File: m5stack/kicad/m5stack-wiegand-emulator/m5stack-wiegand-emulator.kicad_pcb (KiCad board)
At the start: 2 copper layers, 50 x 50 mm, 21 parts, among them J1 2x15 socket header, J2 2x15 pin header, J3 1x5 female, U2 ISOW7841, U3 SN74LVC2G126-EP, U4 TPS62906DRL, U5 SN74AHCT1G125

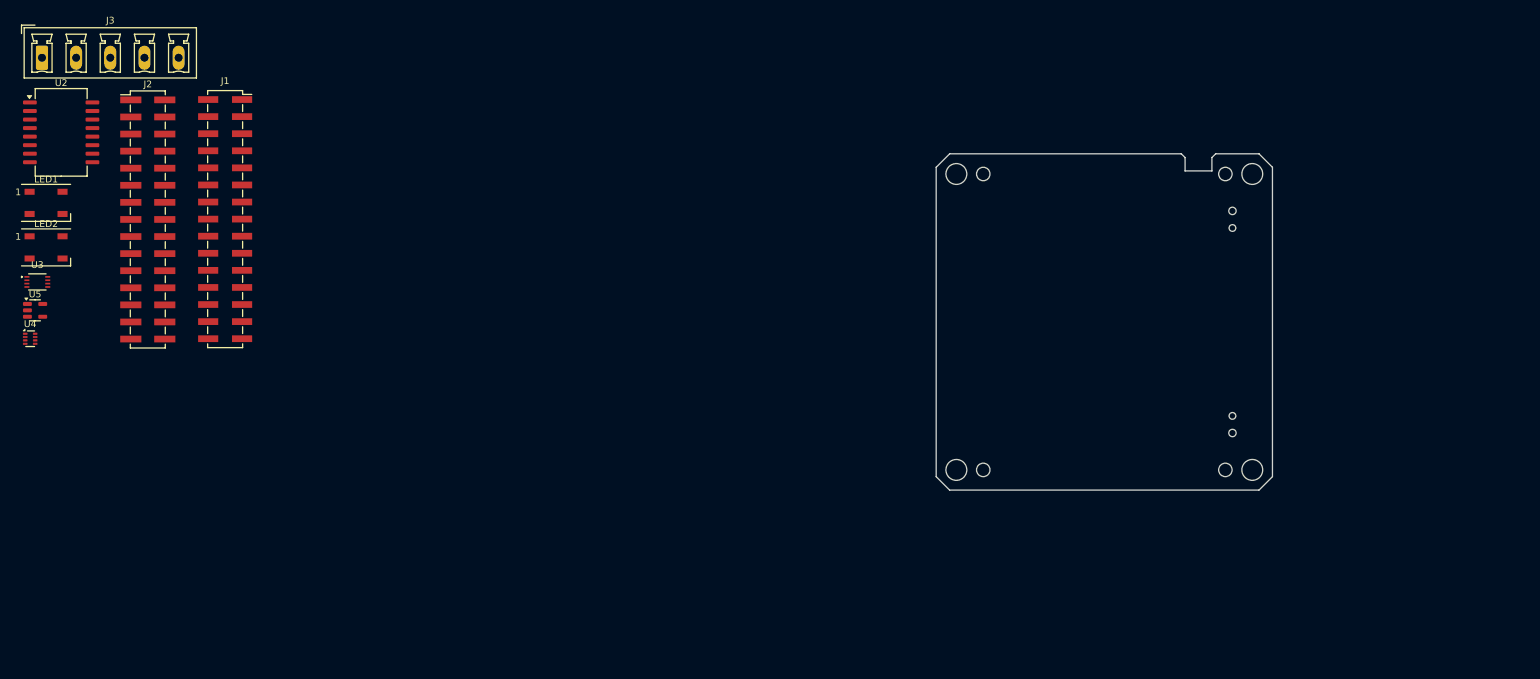
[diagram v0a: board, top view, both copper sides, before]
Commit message: M5: placed J1/J2 connectors
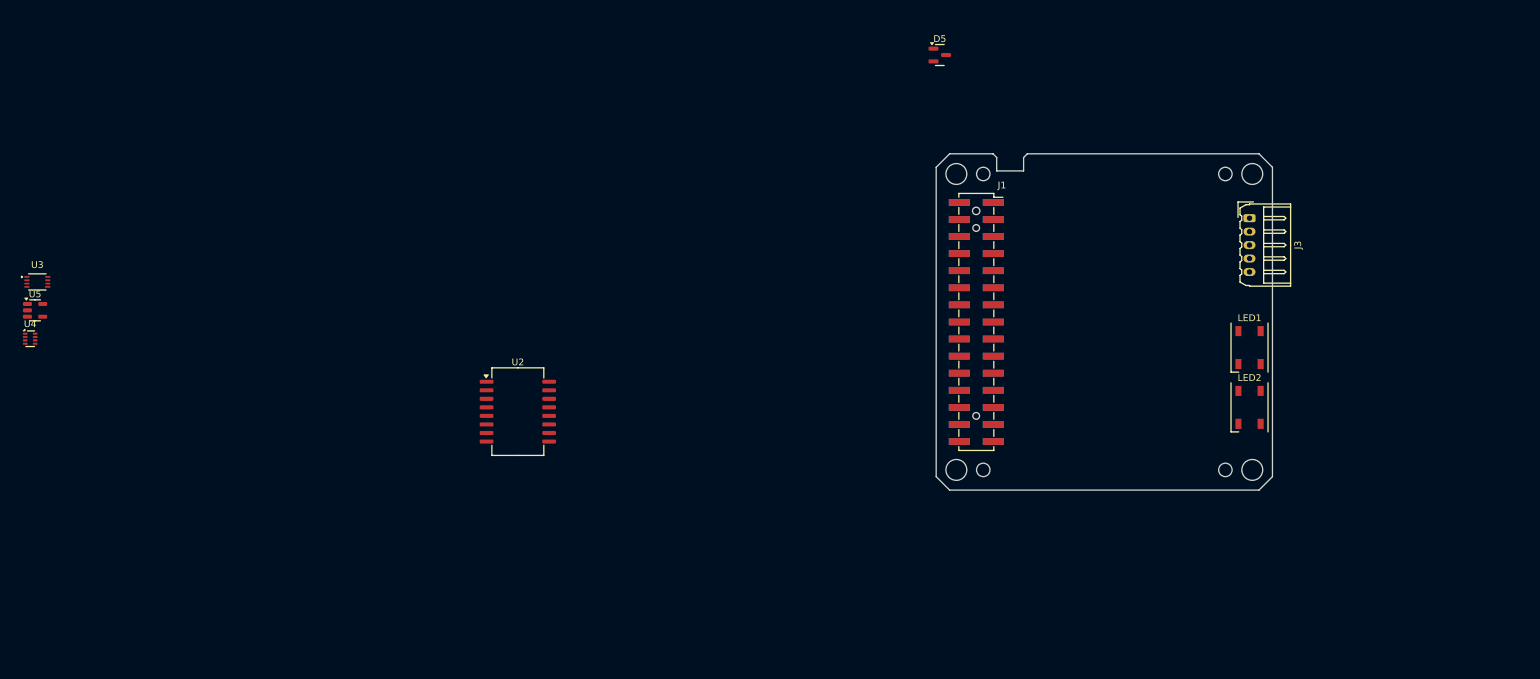
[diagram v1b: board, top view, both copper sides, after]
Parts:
- removed the REF** at (133.3, 105.4)
- added D5: BAT54S, Package_TO_SOT_SMD:SOT-23, F.Cu at (89.8, 49.2)
- J2: moved to B.Cu
- J3: footprint Connector_Phoenix_MC_HighVoltage:PhoenixContact_MCV_1,5_5-G-5.08_1x05_P5.08mm_Vertical -> Connector_Molex:Molex_Micro-Latch_53254-0570_1x05_P2.00mm_Horizontal
- moved J3 181.1 mm to (135.9, 73.5), turned to -90 degrees
- moved LED2 180.5 mm to (135.9, 101.6), turned to -90 degrees
- moved LED1 180.2 mm to (135.9, 92.7), turned to -90 degrees
- moved J2 124.1 mm to (95.3, 88.9), turned to 180 degrees
- moved J1 112.7 mm to (95.3, 88.9)
- moved U2 79.6 mm to (27.1, 102.2)
- moved REF** 38.1 mm to (95.2, 102.9)
- moved REF** 38.1 mm to (95.2, 74.9)
- moved REF** 38.1 mm to (95.2, 72.4)
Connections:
- J1 pad 1: GND -> /ADC1
- J1 pad 10: /DAC1 -> /MISO
- J1 pad 11: /SCLK -> /3V3
- J1 pad 12: /3V3 -> /SCLK
- J1 pad 13: /RXD1 -> /TXD1
- J1 pad 14: /TXD1 -> /RXD1
- J1 pad 15: /RXD2 -> /TXD2
- J1 pad 16: /TXD2 -> /RXD2
- J1 pad 17: /SDA -> /SCL
- J1 pad 18: /SCL -> /SDA
- J1 pad 19: /IO6 -> /IO7
- J1 pad 2: /ADC1 -> GND
- J1 pad 20: /IO7 -> /IO6
- J1 pad 21: /IO8 -> /IO9
- J1 pad 22: /IO9 -> /IO8
- J1 pad 23: /IO10 -> /IO11
- J1 pad 24: /IO11 -> /IO10
- J1 pad 25: /HPWR -> /ADC0
- J1 pad 26: /ADC0 -> /HPWR
- J1 pad 27: /HPWR -> /5VDC
- J1 pad 28: /5VDC -> /HPWR
- J1 pad 29: /HPWR -> /BATTERY
- J1 pad 3: GND -> /ADC2
- J1 pad 30: /BATTERY -> /HPWR
- J1 pad 4: /ADC2 -> GND
- J1 pad 5: GND -> /RESET
- J1 pad 6: /RESET -> GND
- J1 pad 7: /MOSI -> /DAC0
- J1 pad 8: /DAC0 -> /MOSI
- J1 pad 9: /MISO -> /DAC1
- J2 pad 1: GND -> /ADC1
- J2 pad 10: /DAC1 -> /MISO
- J2 pad 11: /SCLK -> /3V3
- J2 pad 12: /3V3 -> /SCLK
- J2 pad 13: /RXD1 -> /TXD1
- J2 pad 14: /TXD1 -> /RXD1
- J2 pad 15: /RXD2 -> /TXD2
- J2 pad 16: /TXD2 -> /RXD2
- J2 pad 17: /SDA -> /SCL
- J2 pad 18: /SCL -> /SDA
- J2 pad 19: /IO6 -> /IO7
- J2 pad 2: /ADC1 -> GND
- J2 pad 20: /IO7 -> /IO6
- J2 pad 21: /IO8 -> /IO9
- J2 pad 22: /IO9 -> /IO8
- J2 pad 23: /IO10 -> /IO11
- J2 pad 24: /IO11 -> /IO10
- J2 pad 25: /HPWR -> /ADC0
- J2 pad 26: /ADC0 -> /HPWR
- J2 pad 27: /HPWR -> /5VDC
- J2 pad 28: /5VDC -> /HPWR
- J2 pad 29: /HPWR -> /BATTERY
- J2 pad 3: GND -> /ADC2
- J2 pad 30: /BATTERY -> /HPWR
- J2 pad 4: /ADC2 -> GND
- J2 pad 5: GND -> /RESET
- J2 pad 6: /RESET -> GND
- J2 pad 7: /MOSI -> /DAC0
- J2 pad 8: /DAC0 -> /MOSI
- J2 pad 9: /MISO -> /DAC1
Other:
- outline, holes or cut-outs redrawn

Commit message: M5: adding missing footprints
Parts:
- removed LED2: WS2812B, LED_SMD:LED_WS2812B_PLCC4_5.0x5.0mm_P3.2mm
- added C2: 10nF, Capacitor_SMD:C_0805_2012Metric_Pad1.18x1.45mm_HandSolder, F.Cu at (113.0, 82.5)
- added C3: 10nF, Capacitor_SMD:C_0805_2012Metric_Pad1.18x1.45mm_HandSolder, F.Cu at (113.0, 85.1)
- added C4: 0.1uF, Capacitor_SMD:C_0805_2012Metric_Pad1.18x1.45mm_HandSolder, F.Cu at (108.0, 82.5)
- added C5: 0.1uF, Capacitor_SMD:C_0805_2012Metric_Pad1.18x1.45mm_HandSolder, F.Cu at (108.0, 85.1)
- added C6: 0.1uF, Capacitor_SMD:C_0805_2012Metric_Pad1.18x1.45mm_HandSolder, F.Cu at (102.9, 85.1)
- added C7: 0.1uF, Capacitor_SMD:C_0805_2012Metric_Pad1.18x1.45mm_HandSolder, F.Cu at (102.9, 82.5)
- added F1: Polyfuse_Small, Fuse:Fuse_Littelfuse-NANO2-451_453, F.Cu at (132.1, 77.6)
- added JP1: Jumper_2_Bridged, Connector_PinHeader_1.27mm:PinHeader_1x02_P1.27mm_Vertical, F.Cu at (102.9, 71.1)
- added JP2: Jumper_3_Bridged12, Connector_PinHeader_1.27mm:PinHeader_1x03_P1.27mm_Vertical, F.Cu at (101.6, 91.4)
- added JP3: Jumper_2_Bridged, Connector_PinHeader_1.27mm:PinHeader_1x02_P1.27mm_Vertical, F.Cu at (102.9, 74.9)
- added JP4: Jumper_3_Bridged12, Connector_PinHeader_1.27mm:PinHeader_1x03_P1.27mm_Vertical, F.Cu at (101.6, 99.1)
- added JP5: Jumper_3_Bridged12, Connector_PinHeader_1.27mm:PinHeader_1x03_P1.27mm_Vertical, F.Cu at (118.1, 83.8)
- added JP6: Jumper_2_Bridged, Connector_PinHeader_1.27mm:PinHeader_1x02_P1.27mm_Vertical, F.Cu at (132.1, 71.1)
- added JP7: Jumper_3_Bridged12, Connector_PinHeader_1.27mm:PinHeader_1x03_P1.27mm_Vertical, F.Cu at (124.5, 83.8)
- added R1: 10k, Resistor_SMD:R_Array_Convex_5x1206, F.Cu at (128.3, 90.2)
- added R10: 470, Resistor_SMD:R_0805_2012Metric_Pad1.20x1.40mm_HandSolder, F.Cu at (133.1, 92.7)
- added R11: 470, Resistor_SMD:R_0805_2012Metric_Pad1.20x1.40mm_HandSolder, F.Cu at (137.2, 87.6)
- added R12: 470, Resistor_SMD:R_0805_2012Metric_Pad1.20x1.40mm_HandSolder, F.Cu at (137.2, 90.2)
- added R13: 10, Resistor_SMD:R_0805_2012Metric_Pad1.20x1.40mm_HandSolder, F.Cu at (137.2, 92.7)
- added R14: 100k, Resistor_SMD:R_0805_2012Metric_Pad1.20x1.40mm_HandSolder, F.Cu at (121.9, 73.7)
- added R15: 100k, Resistor_SMD:R_0805_2012Metric_Pad1.20x1.40mm_HandSolder, F.Cu at (121.7, 76.2)
- added R16: 27k, Resistor_SMD:R_0805_2012Metric_Pad1.20x1.40mm_HandSolder, F.Cu at (121.9, 78.7)
- added R4: 470, Resistor_SMD:R_0805_2012Metric_Pad1.20x1.40mm_HandSolder, F.Cu at (128.3, 109.2)
- added R7: 10k, Resistor_SMD:R_0805_2012Metric_Pad1.20x1.40mm_HandSolder, F.Cu at (128.3, 105.4)
- added R8: 10k, Resistor_SMD:R_0805_2012Metric_Pad1.20x1.40mm_HandSolder, F.Cu at (133.1, 87.6)
- added R9: 10k, Resistor_SMD:R_0805_2012Metric_Pad1.20x1.40mm_HandSolder, F.Cu at (133.1, 90.2)
- added TP1: TestPoint, TestPoint:TestPoint_THTPad_1.0x1.0mm_Drill0.5mm, F.Cu at (129.5, 64.8)
- added TP2: TestPoint, TestPoint:TestPoint_THTPad_1.0x1.0mm_Drill0.5mm, F.Cu at (119.4, 64.8)
- added TP3: TestPoint, TestPoint:TestPoint_THTPad_1.0x1.0mm_Drill0.5mm, F.Cu at (125.7, 64.8)
- added TP4: TestPoint, TestPoint:TestPoint_THTPad_1.0x1.0mm_Drill0.5mm, F.Cu at (100.3, 111.8)
- added U1: RP2040, uhppoted:RP2040-TINY, F.Cu at (114.3, 100.3)
- moved U5 179.5 mm to (134.6, 96.5)
- moved U4 168.5 mm to (121.4, 67.8)
- moved U3 166.7 mm to (121.9, 71.1)
- moved U2 89.4 mm to (111.8, 73.7)
- moved D5 63.3 mm to (129.2, 98.7)
- moved LED1 11.4 mm to (135.5, 104.1)
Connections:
- LED1 pad 2: Net-(LED1-DOUT) -> unconnected-(LED1-DOUT-Pad2)
- U4 pad 2: Net-(JP9-A) -> GND
- U4 pad 7: Net-(JP8-A) -> Net-(D1-K)

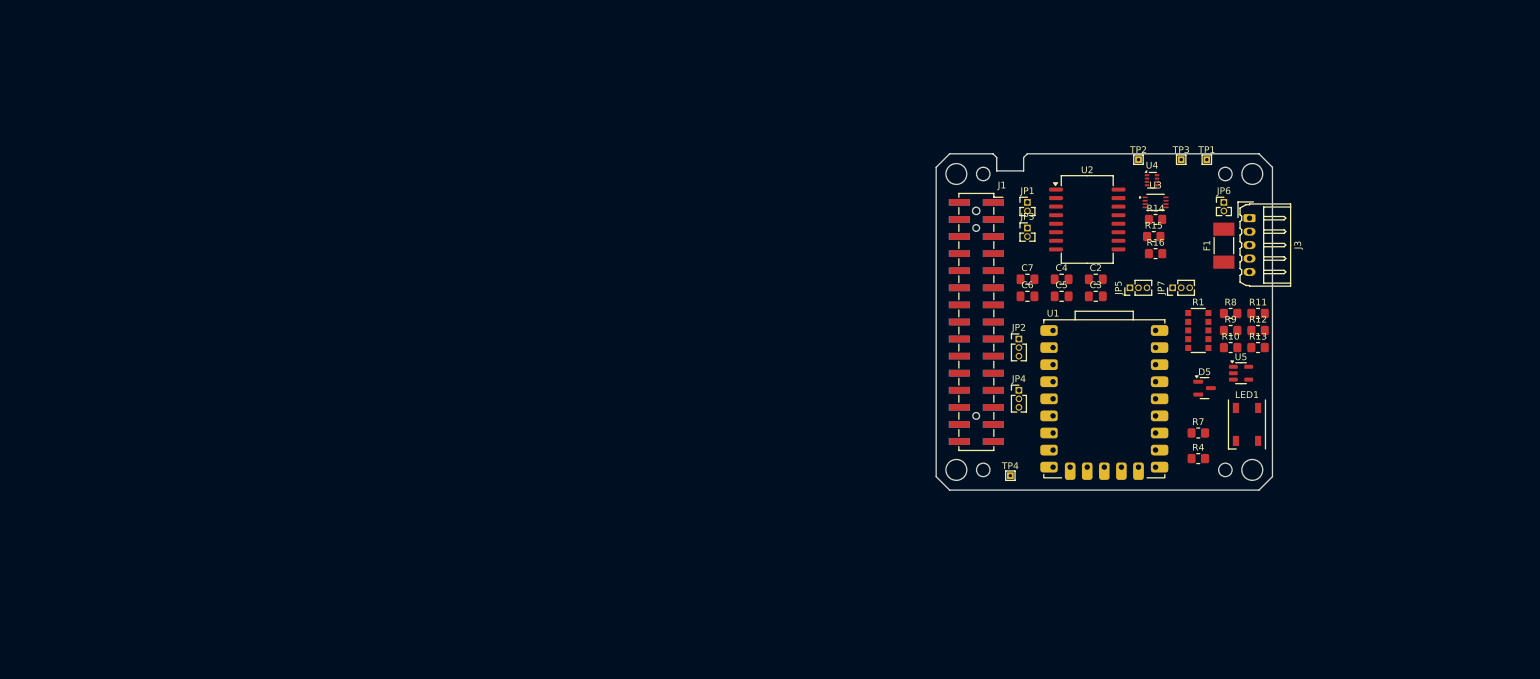
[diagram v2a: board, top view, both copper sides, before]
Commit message: M5: shuffling footprints
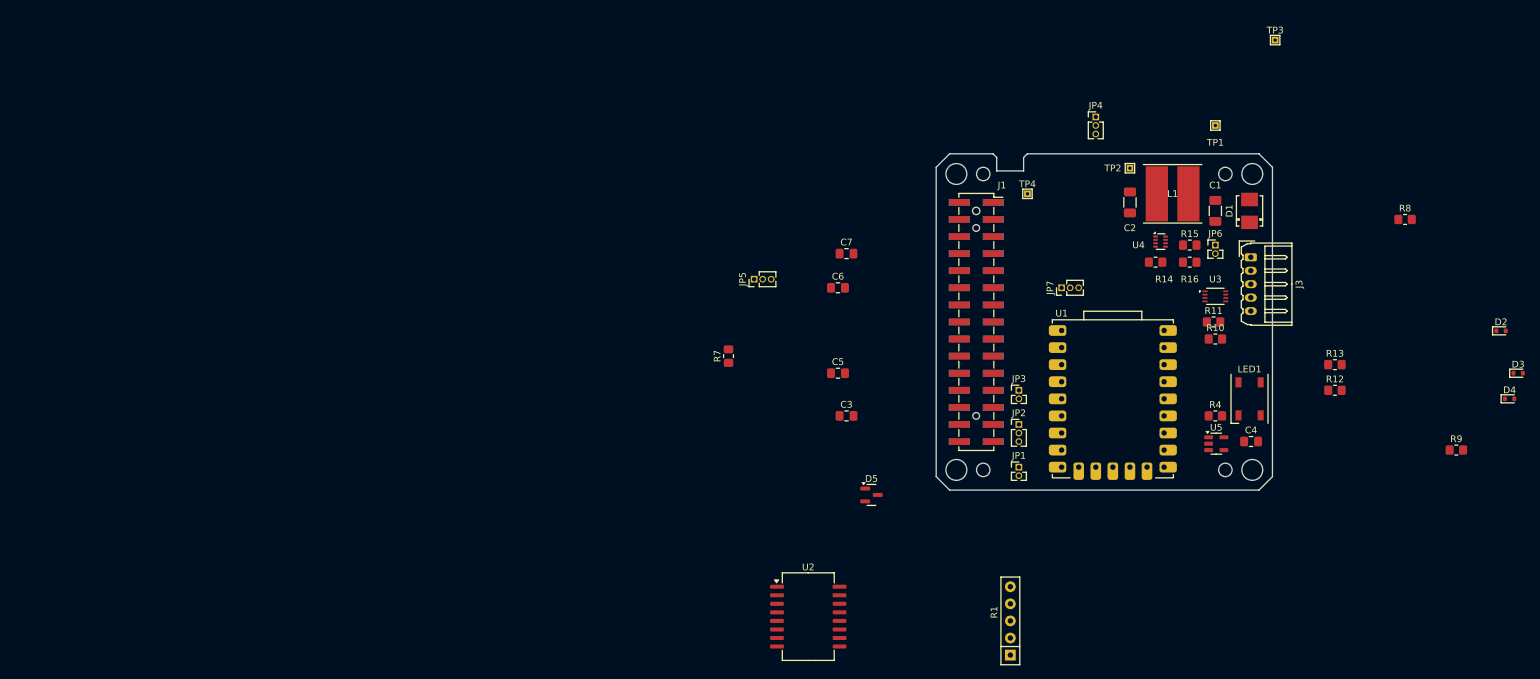
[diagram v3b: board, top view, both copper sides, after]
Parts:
- removed F1: Polyfuse_Small, Fuse:Fuse_Littelfuse-NANO2-451_453
- added C1: 10uF, Capacitor_SMD:C_1206_3216Metric_Pad1.33x1.80mm_HandSolder, F.Cu at (130.8, 72.4)
- added D1: GF1A, uhppoted:DIODE_DO-214BA, F.Cu at (135.9, 72.4)
- added D2: D_TVS, Diode_SMD:D_SOD-523, F.Cu at (173.3, 90.2)
- added D3: D_TVS, Diode_SMD:D_SOD-523, F.Cu at (175.8, 96.5)
- added D4: D_TVS, Diode_SMD:D_SOD-523, F.Cu at (174.6, 100.3)
- added L1: 2.2uH, Inductor_SMD:L_TDK_VLP8040, F.Cu at (124.5, 69.8)
- C2: value 10nF -> 22uF; footprint Capacitor_SMD:C_0805_2012Metric_Pad1.18x1.45mm_HandSolder -> Capacitor_SMD:C_1206_3216Metric_Pad1.33x1.80mm_HandSolder
- R1: footprint Resistor_SMD:R_Array_Convex_5x1206 -> Resistor_THT:R_Array_SIP5
- moved U2 72.2 mm to (70.3, 132.7)
- moved R7 70.8 mm to (58.4, 94.0), turned to 90 degrees
- moved JP5 55.9 mm to (62.2, 82.5)
- moved R1 55.8 mm to (100.3, 138.4), turned to 90 degrees
- moved D5 52.0 mm to (79.7, 114.6)
- moved JP4 42.2 mm to (113.0, 58.4)
- moved TP4 42.0 mm to (102.9, 69.8)
- moved C3 41.1 mm to (76.0, 102.9)
- moved JP1 39.4 mm to (101.6, 110.5)
- moved R9 38.0 mm to (166.6, 108.0)
- moved C4 37.1 mm to (136.1, 106.7)
- moved C5 35.2 mm to (74.7, 96.5)
- moved R8 29.5 mm to (159.0, 73.7)
- moved C6 28.2 mm to (74.7, 83.8)
- moved C7 27.2 mm to (76.0, 78.7)
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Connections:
- C2 pad 1: Net-(U2-IND) -> +VDC

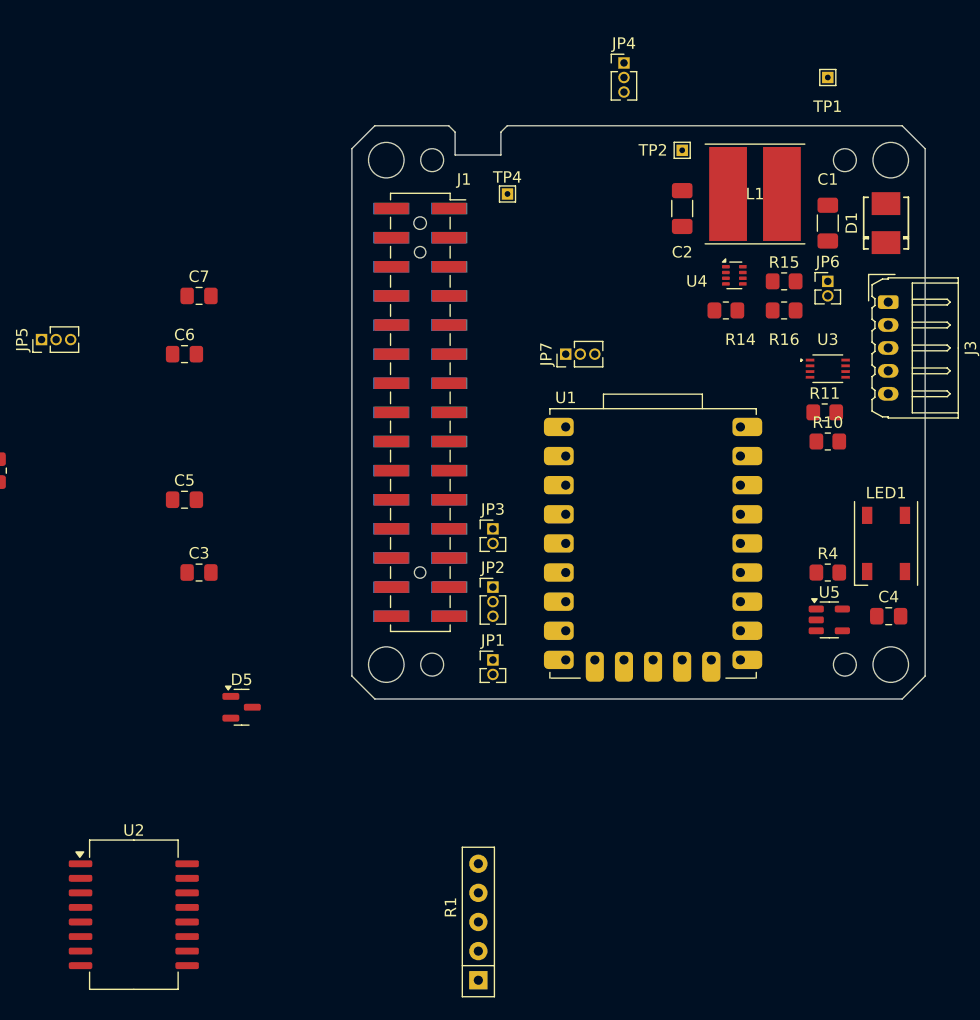
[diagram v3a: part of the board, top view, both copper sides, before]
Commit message: M5: changed L1 footprint to Vishay/1210
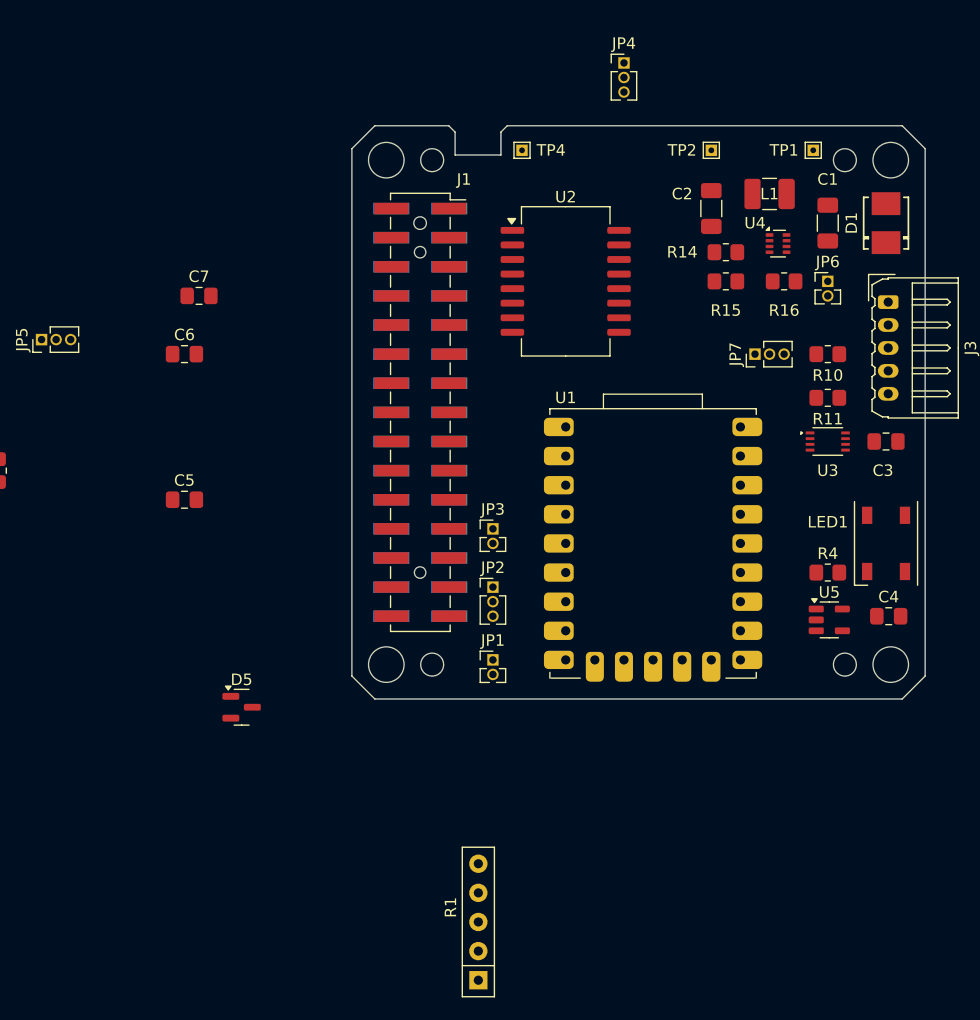
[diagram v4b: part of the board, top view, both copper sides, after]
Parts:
- L1: footprint Inductor_SMD:L_TDK_VLP8040 -> Inductor_SMD:L_1210_3225Metric_Pad1.42x2.65mm_HandSolder
- moved U2 66.9 mm to (108.0, 77.5)
- moved C3 61.0 mm to (135.9, 91.4)
- moved JP7 16.5 mm to (124.5, 83.8)
- moved R10 7.62 mm to (130.8, 83.8)
- moved TP1 6.48 mm to (129.5, 66.0)
- moved U3 6.35 mm to (130.8, 91.4)
- moved R14 5.08 mm to (121.9, 74.9), turned to 180 degrees
- moved R15 5.08 mm to (121.9, 77.5)
- moved U4 4.71 mm to (126.5, 74.2)
- moved TP4 4.02 mm to (104.1, 66.0)
- moved C2 2.54 mm to (120.7, 71.1)
- moved R16 2.54 mm to (127.0, 77.5)
- moved TP2 2.54 mm to (120.7, 66.0)
- moved R11 1.30 mm to (130.8, 87.6)
- moved L1 1.27 mm to (125.7, 69.8)
